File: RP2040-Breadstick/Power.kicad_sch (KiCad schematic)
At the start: 15 parts, among them J501 Conn_01x01, J502 Conn_01x01, J503 Conn_01x01, J504 Conn_01x01, J505 Conn_01x01, J506 Conn_01x01, U501 AZ1117R-3.3TRE1

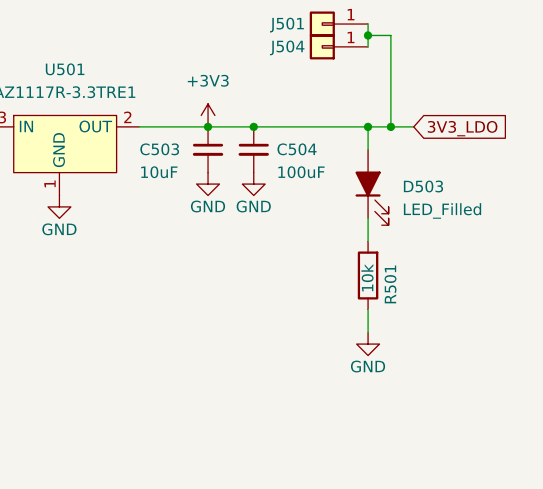
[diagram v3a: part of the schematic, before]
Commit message: Made USB Resistors and Crystal Caps 0201
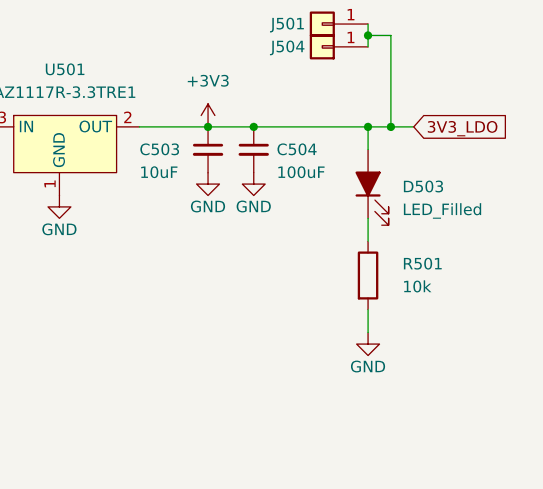
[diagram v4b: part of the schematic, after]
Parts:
- R501: footprint Breadstick Footprints:Perfect_0402_Resistor -> Breadstick Footprints:Perfect_0201_Resistor; JLCPCB P/N C25744 -> C2092258
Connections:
- net GND: now also R501.2; no longer R501.1
- net at D503.1 (K): now also R501.1; no longer R501.2
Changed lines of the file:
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@@
-    (pin "2")
-  )
-  (symbol (lib_id "Device:R") (at 186.69 111.76 180) (unit 1)
-    (in_bom yes) (on_board yes)
-    (property "Reference" "R501" (id 0) (at 189.23 110.49 90)
-      (effects (font (size 1.27 1.27)) (justify left))
-    )
-    (property "Value" "10k" (id 1) (at 186.69 110.49 90)
-      (effects (font (size 1.27 1.27)) (justify left))
-    )
-    (property "Footprint" "Breadstick Footprints:Perfect_0402_Resistor" (id 2) (at 188.468 111.76 90)
-      (effects (font (size 1.27 1.27)) hide)
-    )
-    (property "Datasheet" "~" (id 3) (at 186.69 111.76 0)
-      (effects (font (size 1.27 1.27)) hide)
-    )
-    (property "JLCPCB P/N" "C25744" (id 4) (at 186.69 111.76 0)
-      (effects (font (size 1.27 1.27)) hide)
-    )
-    (pin "1")
     (pin "2")
   )
@@
     (pin "1")
   )
+  (symbol (lib_id "Device:R") (at 186.69 111.76 0) (unit 1)
+    (in_bom yes) (on_board yes) (fields_autoplaced)
+    (property "Reference" "R501" (id 0) (at 190.5 110.4899 0)
+      (effects (font (size 1.27 1.27)) (justify left))
+    )
+    (property "Value" "10k" (id 1) (at 190.5 113.0299 0)
+      (effects (font (size 1.27 1.27)) (justify left))
+    )
+    (property "Footprint" "Breadstick Footprints:Perfect_0201_Resistor" (id 2) (at 184.912 111.76 90)
+      (effects (font (size 1.27 1.27)) hide)
+    )
+    (property "Datasheet" "~" (id 3) (at 186.69 111.76 0)
+      (effects (font (size 1.27 1.27)) hide)
+    )
+    (property "JLCPCB P/N" "C2092258" (id 4) (at 186.69 111.76 0)
+      (effects (font (size 1.27 1.27)) hide)
+    )
+    (pin "1")
+    (pin "2")
+  )
   (symbol (lib_id "power:+3V3") (at 168.91 95.25 0) (unit 1)

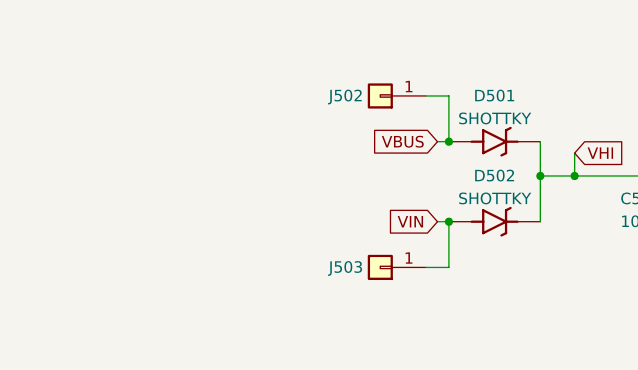
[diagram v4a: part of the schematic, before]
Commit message: Added fuse to VBus, Fixed ESD to allow pasthrough on unused pins, began laying USB and power signals.
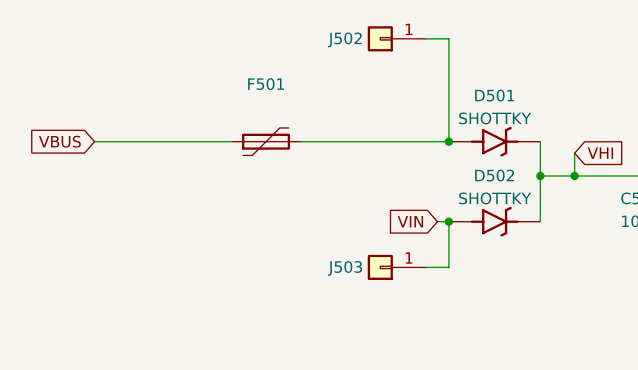
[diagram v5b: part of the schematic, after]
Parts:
- added F501: (no value), symbol Device:Polyfuse
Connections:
- net VBUS: now also F501.1; no longer D501.2 (A), J502.1 (Pin_1)
- new net: D501.2 (A), F501.2, J502.1 (Pin_1)
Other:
- moved on the sheet: J502
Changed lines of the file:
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@@
     (stroke (width 0) (type default) (color 0 0 0 0))
   )
-  (wire (pts (xy 102.87 86.36) (xy 105.41 86.36))
+  (wire (pts (xy 102.87 80.01) (xy 105.41 80.01))
     (stroke (width 0) (type default) (color 0 0 0 0))
   )
@@
     (stroke (width 0) (type default) (color 0 0 0 0))
   )
+  (wire (pts (xy 66.04 91.44) (xy 81.28 91.44))
+    (stroke (width 0) (type default) (color 0 0 0 0))
+  )
   (wire (pts (xy 186.69 95.25) (xy 186.69 97.79))
     (stroke (width 0) (type default) (color 0 0 0 0))
@@
     (stroke (width 0) (type default) (color 0 0 0 0))
   )
-  (wire (pts (xy 104.14 91.44) (xy 105.41 91.44))
+  (wire (pts (xy 88.9 91.44) (xy 105.41 91.44))
     (stroke (width 0) (type default) (color 0 0 0 0))
   )
@@
     (stroke (width 0) (type default) (color 0 0 0 0))
   )
-  (wire (pts (xy 105.41 86.36) (xy 105.41 91.44))
+  (wire (pts (xy 105.41 80.01) (xy 105.41 91.44))
     (stroke (width 0) (type default) (color 0 0 0 0))
   )
@@
     )
   )
-  (global_label "VBUS" (shape input) (at 104.14 91.44 180) (fields_autoplaced)
+  (global_label "VBUS" (shape input) (at 66.04 91.44 180) (fields_autoplaced)
     (effects (font (size 1.27 1.27)) (justify right))
-    (property "Intersheet References" "${INTERSHEET_REFS}" (id 0) (at 96.8283 91.5194 0)
+    (property "Intersheet References" "${INTERSHEET_REFS}" (id 0) (at 58.7283 91.5194 0)
       (effects (font (size 1.27 1.27)) (justify right) hide)
     )
+  )
+  (symbol (lib_id "Device:Polyfuse") (at 85.09 91.44 90) (unit 1)
+    (in_bom yes) (on_board yes) (fields_autoplaced)
+    (property "Reference" "F501" (id 0) (at 85.09 85.09 90))
+    (property "Value" "" (id 1) (at 85.09 87.63 90))
+    (property "Footprint" "" (id 2) (at 90.17 90.17 0)
+      (effects (font (size 1.27 1.27)) (justify left) hide)
+    )
+    (property "Datasheet" "~" (id 3) (at 85.09 91.44 0)
+      (effects (font (size 1.27 1.27)) hide)
+    )
+    (property "JLCPCB P/N" "C70063" (id 4) (at 85.09 91.44 90)
+      (effects (font (size 1.27 1.27)) hide)
+    )
+    (pin "1")
+    (pin "2")
   )
   (symbol (lib_id "Device:C_Small") (at 137.16 97.79 0) (unit 1)
@@
     (pin "1")
   )
-  (symbol (lib_id "Connector_Generic:Conn_01x01") (at 97.79 86.36 180) (unit 1)
-    (in_bom yes) (on_board yes)
-    (property "Reference" "J502" (id 0) (at 93.98 86.36 0))
-    (property "Value" "Conn_01x01" (id 1) (at 87.63 86.36 0)
-      (effects (font (size 1.27 1.27)) hide)
-    )
-    (property "Footprint" "Connector_PinHeader_2.54mm:PinHeader_1x01_P2.54mm_Vertical" (id 2) (at 97.79 86.36 0)
-      (effects (font (size 1.27 1.27)) hide)
-    )
-    (property "Datasheet" "~" (id 3) (at 97.79 86.36 0)
-      (effects (font (size 1.27 1.27)) hide)
-    )
-    (property "JLCPCB P/N" "C492400" (id 4) (at 97.79 86.36 0)
-      (effects (font (size 1.27 1.27)) hide)
-    )
+  (symbol (lib_id "Connector_Generic:Conn_01x01") (at 97.79 80.01 180) (unit 1)
+    (in_bom yes) (on_board yes)
+    (property "Reference" "J502" (id 0) (at 93.98 80.01 0))
+    (property "Value" "Conn_01x01" (id 1) (at 87.63 80.01 0)
+      (effects (font (size 1.27 1.27)) hide)
+    )
+    (property "Footprint" "Connector_PinHeader_2.54mm:PinHeader_1x01_P2.54mm_Vertical" (id 2) (at 97.79 80.01 0)
+      (effects (font (size 1.27 1.27)) hide)
+    )
+    (property "Datasheet" "~" (id 3) (at 97.79 80.01 0)
+      (effects (font (size 1.27 1.27)) hide)
+    )
+    (property "JLCPCB P/N" "C492400" (id 4) (at 97.79 80.01 0)
+      (effects (font (size 1.27 1.27)) hide)
+    )

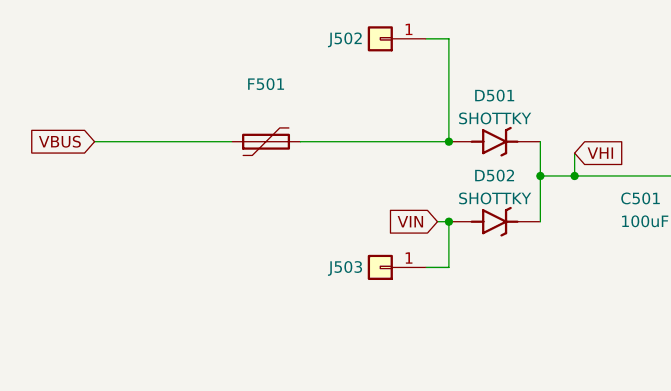
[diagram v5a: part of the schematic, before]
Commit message: Rearranged LDO and Flash IC, routing first half of board.
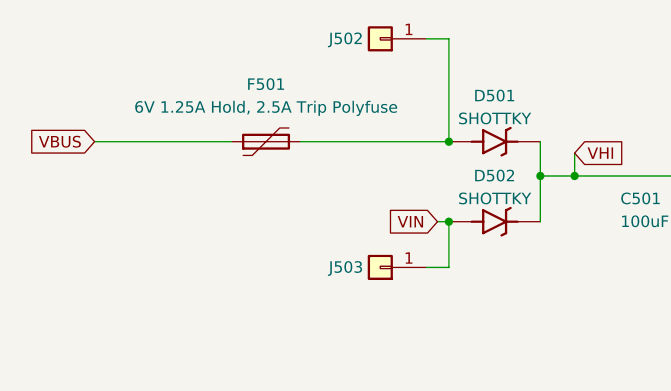
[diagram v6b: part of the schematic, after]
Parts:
- F501: value (none) -> 6V 1.25A Hold, 2.5A Trip Polyfuse; footprint (none) -> Fuse:Fuse_0805_2012Metric
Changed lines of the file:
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@@
     (in_bom yes) (on_board yes) (fields_autoplaced)
     (property "Reference" "F501" (id 0) (at 85.09 85.09 90))
-    (property "Value" "" (id 1) (at 85.09 87.63 90))
-    (property "Footprint" "" (id 2) (at 90.17 90.17 0)
+    (property "Value" "6V 1.25A Hold, 2.5A Trip Polyfuse" (id 1) (at 85.09 87.63 90))
+    (property "Footprint" "Fuse:Fuse_0805_2012Metric" (id 2) (at 90.17 90.17 0)
       (effects (font (size 1.27 1.27)) (justify left) hide)
     )

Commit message: Figuring Out IMU and Level Shifter Routing
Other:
- company: (none) -> J & R Creative Technologies Inc.
- title: (none) -> RP2040 Breadstick
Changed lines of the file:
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@@
 (kicad_sch (version 20211123) (generator eeschema)
   (paper "A4")
+  (title_block
+    (title "RP2040 Breadstick")
+    (date "2022-08-10")
+    (rev "0.1")
+    (company "J & R Creative Technologies Inc.")
+    (comment 1 "@RangenMichael")
+    (comment 2 "https://twitter.com/RangenMichael")
+    (comment 3 "Apache-2.0 License")
+    (comment 4 "https://github.com/mrangen/RP2040-Breadstick")
+  )
   (junction (at 119.38 95.25) (diameter 0) (color 0 0 0 0)
   )

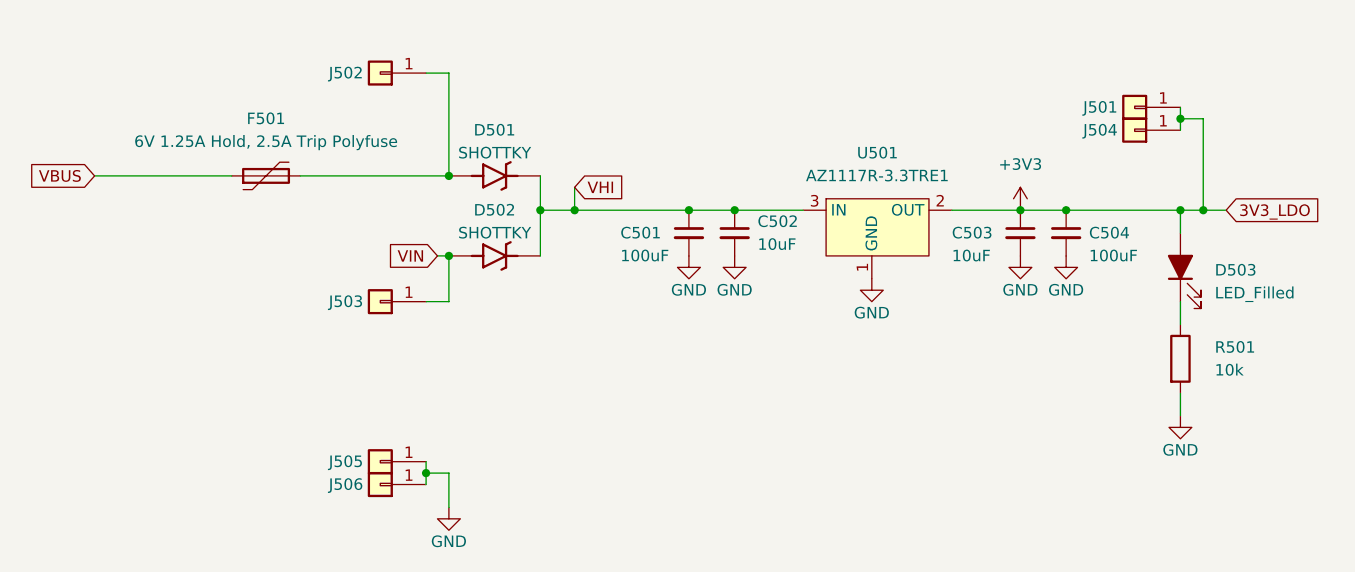
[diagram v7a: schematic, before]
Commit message: Routing to Flash IC done, removed 0402 capacitors from the LDO
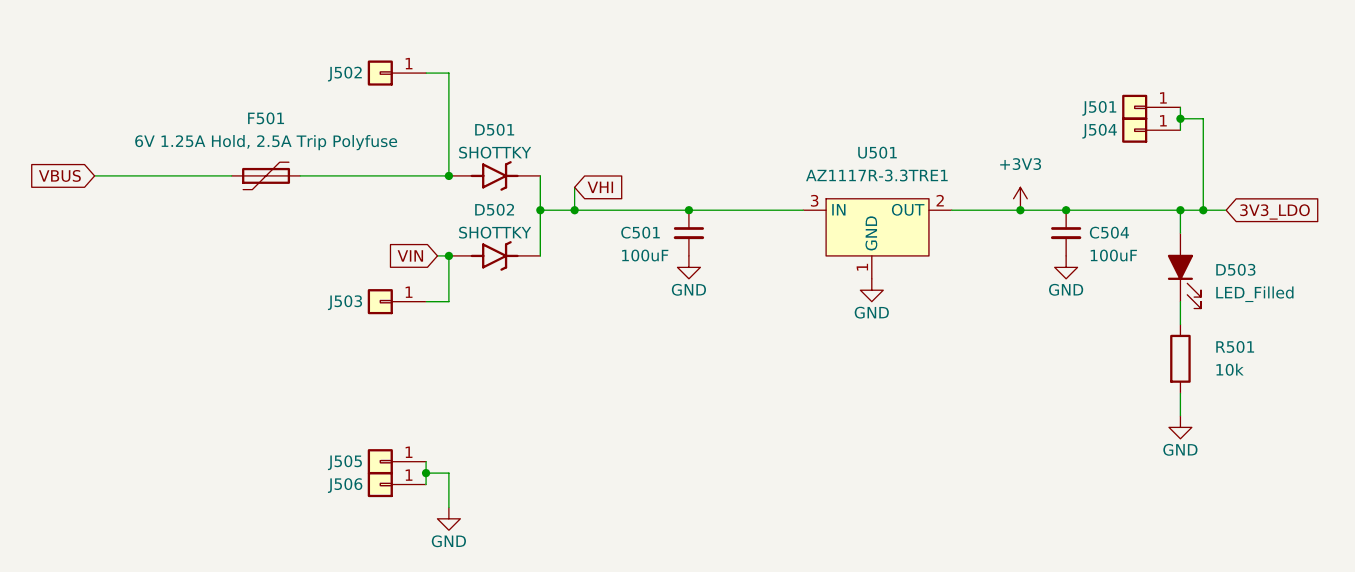
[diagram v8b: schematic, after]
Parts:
- removed C502, C503: 10uF, Breadstick Footprints:Perfect_0402_Cap, symbol Device:C_Small
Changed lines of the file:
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@@
   (junction (at 168.91 95.25) (diameter 0) (color 0 0 0 0)
   )
-  (junction (at 137.16 95.25) (diameter 0) (color 0 0 0 0)
-  )
   (junction (at 105.41 91.44) (diameter 0) (color 0 0 0 0)
   )
@@
     (stroke (width 0) (type default) (color 0 0 0 0))
   )
-  (wire (pts (xy 132.08 95.25) (xy 137.16 95.25))
-    (stroke (width 0) (type default) (color 0 0 0 0))
-  )
-  (wire (pts (xy 137.16 95.25) (xy 144.78 95.25))
+  (wire (pts (xy 132.08 95.25) (xy 144.78 95.25))
     (stroke (width 0) (type default) (color 0 0 0 0))
   )
@@
     (pin "2")
   )
-  (symbol (lib_id "Device:C_Small") (at 137.16 97.79 0) (unit 1)
-    (in_bom yes) (on_board yes)
-    (property "Reference" "C502" (id 0) (at 139.7 96.52 0)
-      (effects (font (size 1.27 1.27)) (justify left))
-    )
-    (property "Value" "10uF" (id 1) (at 139.7 99.06 0)
-      (effects (font (size 1.27 1.27)) (justify left))
-    )
-    (property "Footprint" "Breadstick Footprints:Perfect_0402_Cap" (id 2) (at 137.16 97.79 0)
-      (effects (font (size 1.27 1.27)) hide)
-    )
-    (property "Datasheet" "~" (id 3) (at 137.16 97.79 0)
-      (effects (font (size 1.27 1.27)) hide)
-    )
-    (property "JLCPCB P/N" "C15525" (id 4) (at 137.16 97.79 0)
-      (effects (font (size 1.27 1.27)) hide)
-    )
-    (pin "1")
-    (pin "2")
-  )
   (symbol (lib_id "Connector_Generic:Conn_01x01") (at 97.79 123.19 180) (unit 1)
     (in_bom yes) (on_board yes)
@@
     )
     (pin "1")
-  )
-  (symbol (lib_id "Device:C_Small") (at 168.91 97.79 0) (unit 1)
-    (in_bom yes) (on_board yes)
-    (property "Reference" "C503" (id 0) (at 161.29 97.79 0)
-      (effects (font (size 1.27 1.27)) (justify left))
-    )
-    (property "Value" "10uF" (id 1) (at 161.29 100.33 0)
-      (effects (font (size 1.27 1.27)) (justify left))
-    )
-    (property "Footprint" "Breadstick Footprints:Perfect_0402_Cap" (id 2) (at 168.91 97.79 0)
-      (effects (font (size 1.27 1.27)) hide)
-    )
-    (property "Datasheet" "~" (id 3) (at 168.91 97.79 0)
-      (effects (font (size 1.27 1.27)) hide)
-    )
-    (property "JLCPCB P/N" "C15525" (id 4) (at 168.91 97.79 0)
-      (effects (font (size 1.27 1.27)) hide)
-    )
-    (pin "1")
-    (pin "2")
   )
   (symbol (lib_id "Connector_Generic:Conn_01x01") (at 97.79 105.41 180) (unit 1)
@@
       (effects (font (size 1.27 1.27)) hide)
     )
-    (pin "1")
-  )
-  (symbol (lib_id "power:GND") (at 168.91 100.33 0) (unit 1)
-    (in_bom yes) (on_board yes)
-    (property "Reference" "#PWR0504" (id 0) (at 168.91 106.68 0)
-      (effects (font (size 1.27 1.27)) hide)
-    )
-    (property "Value" "GND" (id 1) (at 168.91 104.14 0))
-    (property "Footprint" "" (id 2) (at 168.91 100.33 0)
-      (effects (font (size 1.27 1.27)) hide)
-    )
-    (property "Datasheet" "" (id 3) (at 168.91 100.33 0)
-      (effects (font (size 1.27 1.27)) hide)
-    )
-    (pin "1")
-  )
-  (symbol (lib_id "power:GND") (at 137.16 100.33 0) (unit 1)
-    (in_bom yes) (on_board yes)
-    (property "Reference" "#PWR0503" (id 0) (at 137.16 106.68 0)
-      (effects (font (size 1.27 1.27)) hide)
-    )
-    (property "Value" "GND" (id 1) (at 137.16 104.14 0))
-    (property "Footprint" "" (id 2) (at 137.16 100.33 0)
-      (effects (font (size 1.27 1.27)) hide)
-    )
-    (property "Datasheet" "" (id 3) (at 137.16 100.33 0)
-      (effects (font (size 1.27 1.27)) hide)
-    )
